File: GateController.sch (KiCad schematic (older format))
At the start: 19 parts, among them K1 RAYEX-L90, K2 RAYEX-L90, M1 N-CHANNEL-MOSFET-BSS138, M2 N-CHANNEL-MOSFET-BSS138, M3 Motor_DC, P1 Power, P2 Analog, P3 Digital, P4 Digital, P5 CONN_01X01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

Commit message: Added pages for power and inputs
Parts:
- removed C1: C_Small, symbol Device:C_Small
- removed D3: DIODE, symbol AM2:DIODE-Microtan_65_CPU-cache
- removed D4: DIODE, symbol pspice:DIODE
- removed R1: R_Small, symbol Device:R_Small
- D1, D2: symbol AM2:DIODE-Microtan_65_CPU-cache -> GateController-rescue:DIODE-Microtan_65_CPU-cache-AM2
- M1, M2: symbol AM1:GeekAmmo_N-CHANNEL-MOSFET-BSS138 -> GateController-rescue:GeekAmmo_N-CHANNEL-MOSFET-BSS138-AM1
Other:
- note removed: "INPUT"
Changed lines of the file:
@@
 $Descr A4 11693 8268
 encoding utf-8
-Sheet 1 1
+Sheet 1 3
 Title ""
 Date "lun. 30 mars 2015"
@@
 	10700 1000 10700 500
 $Comp
-L Device:R_Small R1
-U 1 1 5F5FCCF6
-P 6650 5550
-F 0 "R1" V 6454 5550 50  0000 C CNN
-F 1 "R_Small" V 6545 5550 50  0000 C CNN
-F 2 "" H 6650 5550 50  0001 C CNN
-F 3 "~" H 6650 5550 50  0001 C CNN
-	1    6650 5550
-	0    -1   1    0
-$EndComp
-$Comp
-L AM2:DIODE-Microtan_65_CPU-cache D3
-U 1 1 5F5FD3D3
-P 6250 5250
-F 0 "D3" V 6288 5172 40  0000 R CNN
-F 1 "DIODE" V 6212 5172 40  0000 R CNN
-F 2 "" H 6250 5250 60  0001 C CNN
-F 3 "" H 6250 5250 60  0000 C CNN
-	1    6250 5250
-	0    1    -1   0
-$EndComp
-$Comp
-L power:+5V #PWR0102
-U 1 1 5F5FE717
-P 6250 4850
-F 0 "#PWR0102" H 6250 4700 50  0001 C CNN
-F 1 "+5V" H 6265 5023 50  0000 C CNN
-F 2 "" H 6250 4850 50  0001 C CNN
-F 3 "" H 6250 4850 50  0001 C CNN
-	1    6250 4850
-	-1   0    0    -1
-$EndComp
-$Comp
-L Device:C_Small C1
-U 1 1 5F5FEC7A
-P 5700 5900
-F 0 "C1" H 5792 5946 50  0000 L CNN
-F 1 "C_Small" H 5792 5855 50  0000 L CNN
-F 2 "" H 5700 5900 50  0001 C CNN
-F 3 "~" H 5700 5900 50  0001 C CNN
-	1    5700 5900
-	-1   0    0    -1
-$EndComp
-Wire Wire Line
-	6550 5550 6250 5550
-Wire Wire Line
-	6250 5550 6250 5450
-Connection ~ 6250 5550
-Wire Wire Line
-	6250 5050 6250 4850
-Wire Wire Line
-	6250 5550 5700 5550
-Wire Wire Line
-	5700 5550 5700 5800
-$Comp
-L AM1:Microtan_65_CPU-cache_GND #PWR0103
-U 1 1 5F5FFCD8
-P 5700 6300
-F 0 "#PWR0103" H 5700 6300 30  0001 C CNN
-F 1 "Microtan_65_CPU-cache_GND" H 5700 6230 30  0001 C CNN
-F 2 "" H 5700 6300 60  0000 C CNN
-F 3 "" H 5700 6300 60  0000 C CNN
-	1    5700 6300
-	-1   0    0    -1
-$EndComp
-$Comp
 L Relay:RAYEX-L90 K1
 U 1 1 5F6004E4
@@
 	4200 3150 4050 3150
 $Comp
-L AM2:DIODE-Microtan_65_CPU-cache D1
+L GateController-rescue:DIODE-Microtan_65_CPU-cache-AM2 D1
 U 1 1 5F60A460
 P 3650 2550
@@
 $EndComp
 $Comp
-L AM2:DIODE-Microtan_65_CPU-cache D2
+L GateController-rescue:DIODE-Microtan_65_CPU-cache-AM2 D2
 U 1 1 5F60ADB2
 P 6000 2500
@@
 	6600 3150 6400 3150
 $Comp
-L AM1:GeekAmmo_N-CHANNEL-MOSFET-BSS138 M2
+L GateController-rescue:GeekAmmo_N-CHANNEL-MOSFET-BSS138-AM1 M2
 U 1 1 5F60E051
 P 2100 3400
@@
 $EndComp
 $Comp
-L AM1:GeekAmmo_N-CHANNEL-MOSFET-BSS138 M1
+L GateController-rescue:GeekAmmo_N-CHANNEL-MOSFET-BSS138-AM1 M1
 U 1 1 5F610BFB
 P 1350 3350
@@
 	4200 1850 4200 2550
 Connection ~ 6600 2500
-Text Notes 5900 5050 2    50   ~ 0
-INPUT
 Text Notes 3450 1700 0    50   ~ 0
 MOTOR\nCONTROL
-Wire Wire Line
-	5700 5550 4150 5550
-Connection ~ 5700 5550
-Wire Wire Line
-	6750 5550 7450 5550
 Wire Wire Line
 	1900 3500 1900 4300
@@
 Text Label 4150 5450 0    50   ~ 0
 2
-Text Label 4150 5550 0    50   ~ 0
-5(**)
-Text Label 7450 5550 0    50   ~ 0
-MAGICEYE
 Wire Wire Line
 	4850 1700 4200 1700
@@
 NoConn ~ 8900 2800
 $Comp
-L power:PWR_FLAG #FLG0102
-U 1 1 5F7E15C6
-P 7450 5250
-F 0 "#FLG0102" H 7450 5325 50  0001 C CNN
-F 1 "PWR_FLAG" H 7450 5423 50  0000 C CNN
-F 2 "" H 7450 5250 50  0001 C CNN
-F 3 "~" H 7450 5250 50  0001 C CNN
-	1    7450 5250
-	1    0    0    -1
-$EndComp
-Wire Wire Line
-	7450 5250 7450 5550
-$Comp
 L power:PWR_FLAG #FLG0103
 U 1 1 5F7E9261
@@
 Wire Wire Line
 	10300 3150 10300 3200
-Wire Wire Line
-	6250 5550 6250 5650
-$Comp
-L pspice:DIODE D4
-U 1 1 5F5FD987
-P 6250 5850
-F 0 "D4" V 6288 5772 40  0000 R CNN
-F 1 "DIODE" V 6212 5772 40  0000 R CNN
-F 2 "" H 6250 5850 60  0001 C CNN
-F 3 "" H 6250 5850 60  0000 C CNN
-	1    6250 5850
-	0    1    -1   0
-$EndComp
-Wire Wire Line
-	6250 6050 6250 6300
-$Comp
-L AM1:Microtan_65_CPU-cache_GND #PWR0101
-U 1 1 5F5FE1C8
-P 6250 6300
-F 0 "#PWR0101" H 6250 6300 30  0001 C CNN
-F 1 "Microtan_65_CPU-cache_GND" H 6250 6230 30  0001 C CNN
-F 2 "" H 6250 6300 60  0000 C CNN
-F 3 "" H 6250 6300 60  0000 C CNN
-	1    6250 6300
-	-1   0    0    -1
-$EndComp
 $Comp
 L power:PWR_FLAG #FLG0106
@@
 Wire Wire Line
 	6150 7350 6150 7650
-Wire Wire Line
-	5700 6000 5700 6300
 $Comp
 L power:GNDPWR #PWR0111
@@
 	1    0    0    -1
 $EndComp
+$Sheet
+S 8700 3650 850  550
+U 5F62F258
+F0 "Sheet5F62F257" 50
+F1 "gate_ctrl_inputs.sch" 50
+$EndSheet
+$Sheet
+S 8750 4550 850  550
+U 5F648DDC
+F0 "Sheet5F648DDB" 50
+F1 "gate_ctrl_power.sch" 50
+$EndSheet
 $EndSCHEMATC

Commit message: Added outputs page, leds.
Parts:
- added D? (x2): LED, symbol Device:LED
- added R? (x2): R_Small, symbol Device:R_Small
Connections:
- net +24V: now also D?.1 (K), D?.1 (K)
- net at D1.1 (A), K1.A1, M2.3 (D): now also R?.2
- net at D2.1 (A), K2.A2, M1.3 (D): now also R?.2
- new net: D?.2 (A), R?.1 (x2)
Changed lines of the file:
@@
 $Descr A4 11693 8268
 encoding utf-8
-Sheet 1 3
+Sheet 1 4
 Title ""
 Date "lun. 30 mars 2015"
@@
 	4200 1850 6600 1850
 Wire Wire Line
-	6600 1850 6600 2500
+	6600 1850 6600 2200
 Connection ~ 4200 1850
 Wire Wire Line
-	4200 1850 4200 2550
+	4200 1850 4200 2000
 Connection ~ 6600 2500
 Text Notes 3450 1700 0    50   ~ 0
@@
 F1 "gate_ctrl_power.sch" 50
 $EndSheet
+$Sheet
+S 8850 5400 950  550
+U 5F669EA7
+F0 "Sheet5F669EA6" 50
+F1 "gate_ctrl_outputs.sch" 50
+$EndSheet
+$Comp
+L Device:LED D?
+U 1 1 5F682773
+P 6250 2200
+F 0 "D?" H 6243 1945 50  0000 C CNN
+F 1 "LED" H 6243 2036 50  0000 C CNN
+F 2 "" H 6250 2200 50  0001 C CNN
+F 3 "~" H 6250 2200 50  0001 C CNN
+	1    6250 2200
+	-1   0    0    1
+$EndComp
+$Comp
+L Device:LED D?
+U 1 1 5F6837F7
+P 3950 2000
+F 0 "D?" H 3943 1745 50  0000 C CNN
+F 1 "LED" H 3943 1836 50  0000 C CNN
+F 2 "" H 3950 2000 50  0001 C CNN
+F 3 "~" H 3950 2000 50  0001 C CNN
+	1    3950 2000
+	-1   0    0    1
+$EndComp
+Wire Wire Line
+	4100 2000 4200 2000
+Connection ~ 4200 2000
+Wire Wire Line
+	4200 2000 4200 2550
+Wire Wire Line
+	6400 2200 6600 2200
+Connection ~ 6600 2200
+Wire Wire Line
+	6600 2200 6600 2500
+$Comp
+L Device:R_Small R?
+U 1 1 5F68A7C5
+P 5800 2200
+F 0 "R?" V 5604 2200 50  0000 C CNN
+F 1 "R_Small" V 5695 2200 50  0000 C CNN
+F 2 "" H 5800 2200 50  0001 C CNN
+F 3 "~" H 5800 2200 50  0001 C CNN
+	1    5800 2200
+	0    1    1    0
+$EndComp
+$Comp
+L Device:R_Small R?
+U 1 1 5F68B356
+P 3500 2000
+F 0 "R?" V 3304 2000 50  0000 C CNN
+F 1 "R_Small" V 3395 2000 50  0000 C CNN
+F 2 "" H 3500 2000 50  0001 C CNN
+F 3 "~" H 3500 2000 50  0001 C CNN
+	1    3500 2000
+	0    1    1    0
+$EndComp
+Wire Wire Line
+	3600 2000 3800 2000
+Wire Wire Line
+	3400 2000 3150 2000
+Wire Wire Line
+	3150 2000 3150 2550
+Connection ~ 3150 2550
+Wire Wire Line
+	6100 2200 5900 2200
+Wire Wire Line
+	5700 2200 5500 2200
+Wire Wire Line
+	5500 2200 5500 2500
+Connection ~ 5500 2500
 $EndSCHEMATC

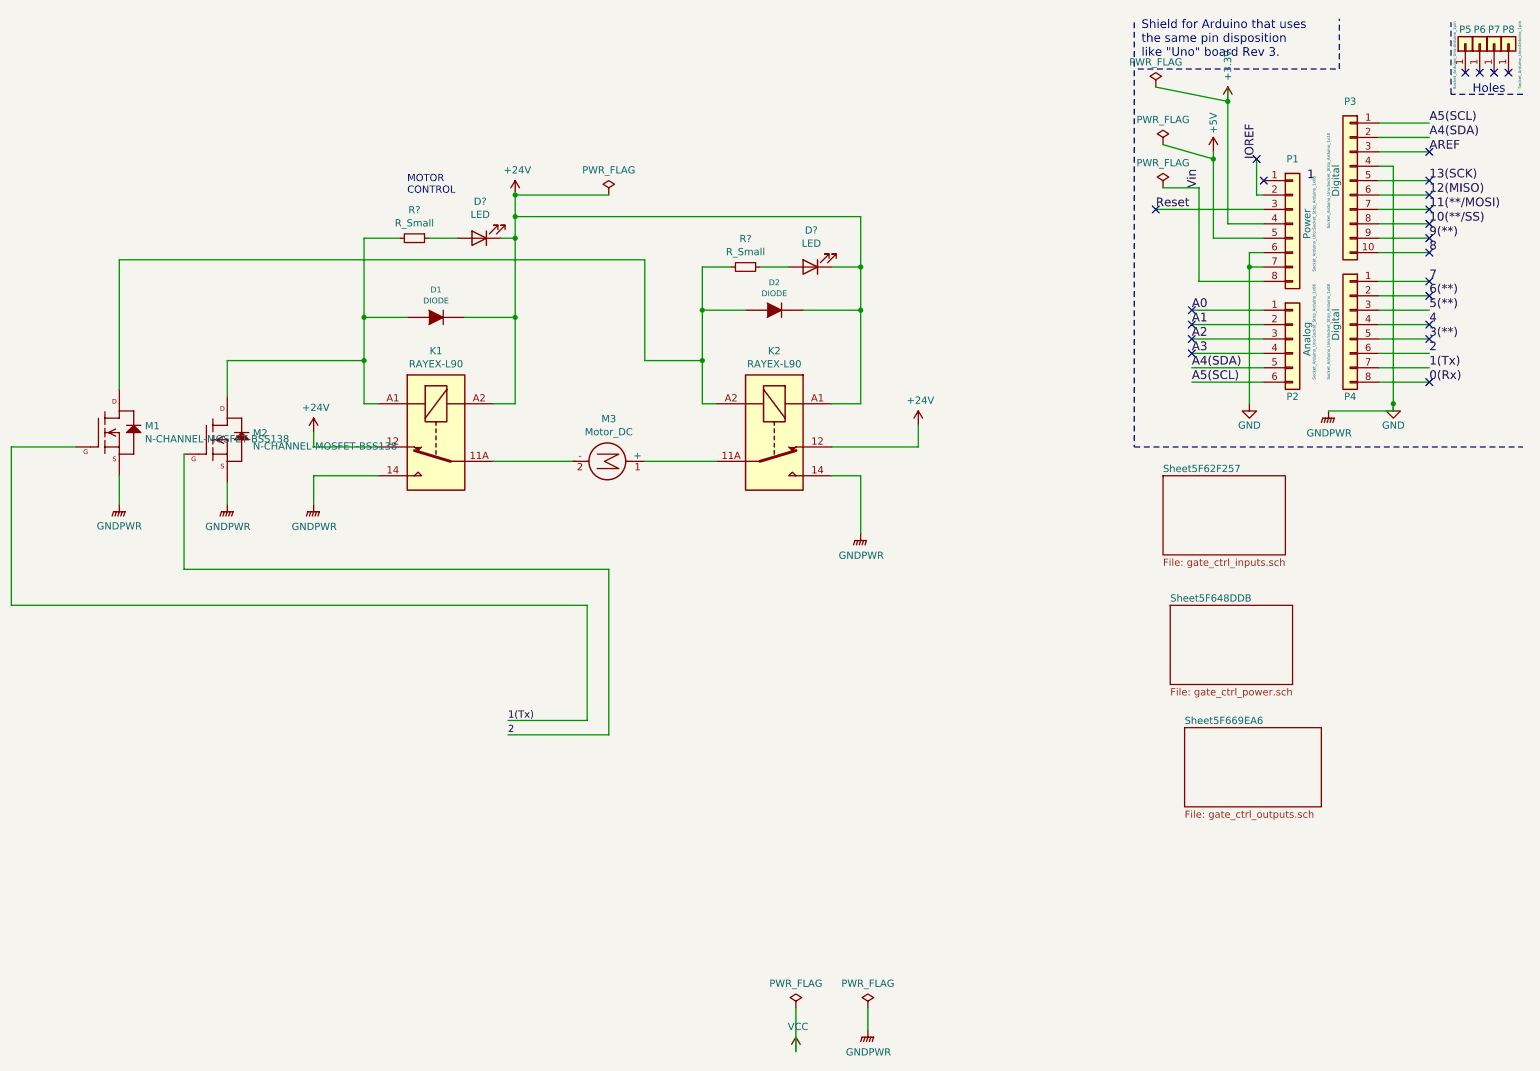
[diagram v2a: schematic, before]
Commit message: Added OLED and RF data input
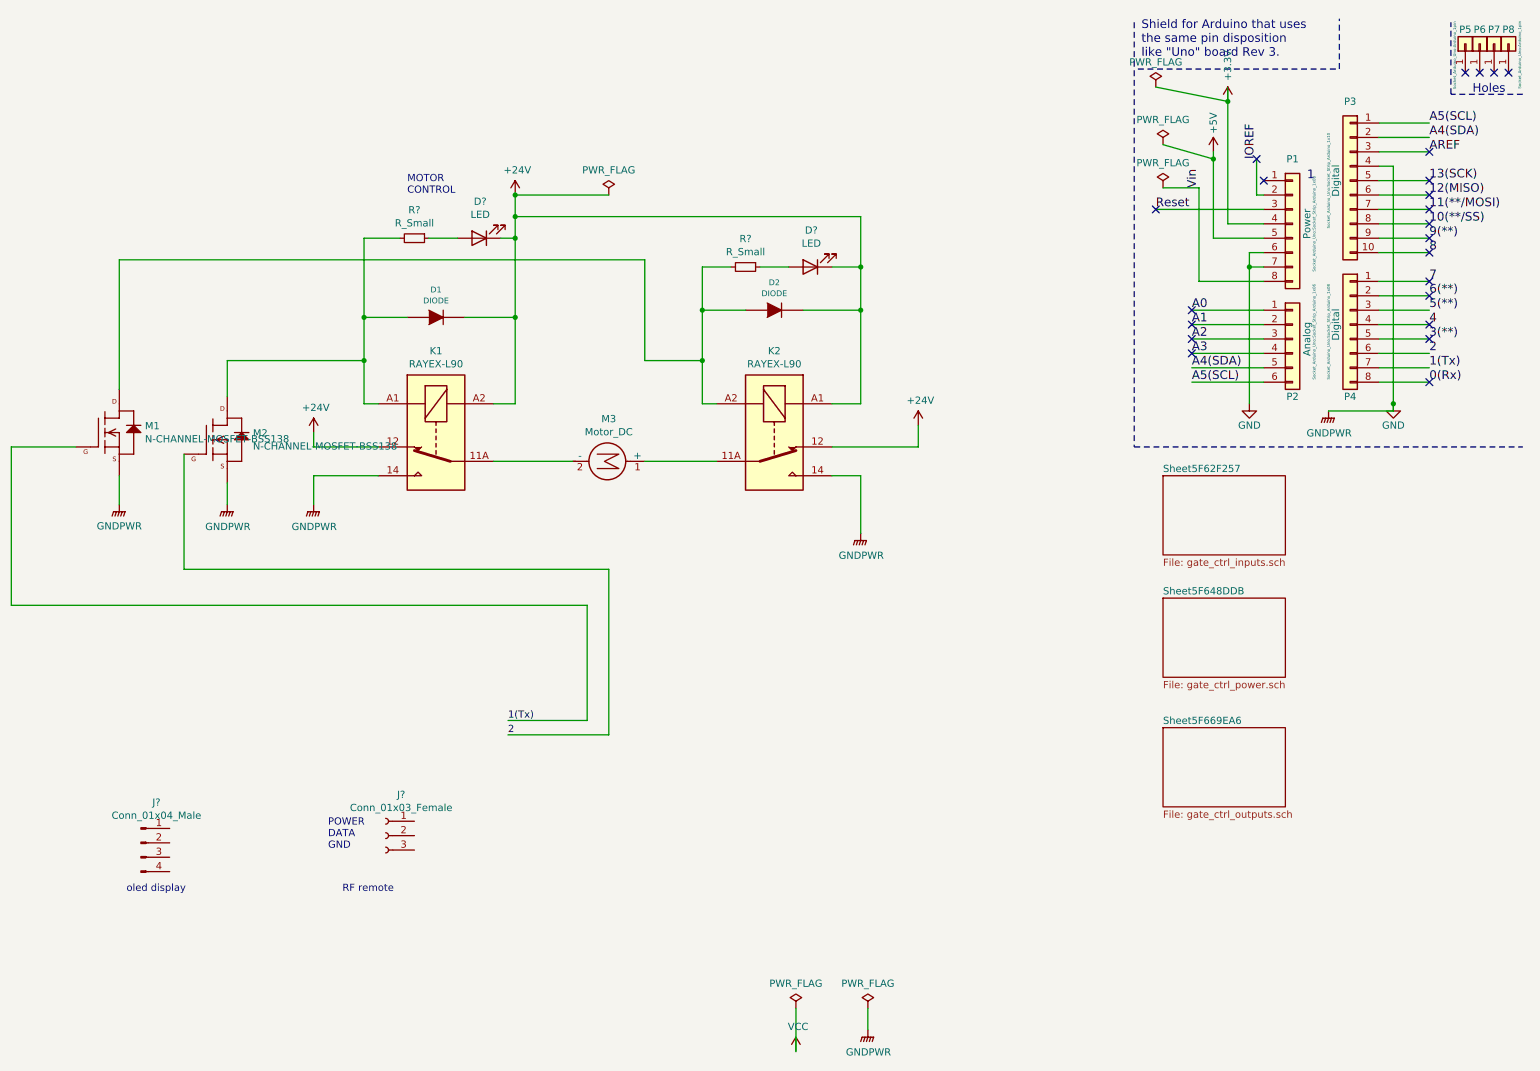
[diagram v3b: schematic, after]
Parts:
- added J?: Conn_01x04_Male, symbol Connector:Conn_01x04_Male
- added J?: Conn_01x03_Female, symbol Connector:Conn_01x03_Female
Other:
- note added: "POWER\nDATA\nGND"
- note added: "RF remote\n"
- note added: "oled display"
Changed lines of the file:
@@
 $EndSheet
 $Sheet
-S 8750 4550 850  550
+S 8700 4500 850  550
 U 5F648DDC
 F0 "Sheet5F648DDB" 50
@@
 $EndSheet
 $Sheet
-S 8850 5400 950  550
+S 8700 5400 850  550
 U 5F669EA7
 F0 "Sheet5F669EA6" 50
@@
 	5500 2200 5500 2500
 Connection ~ 5500 2500
+$Comp
+L Connector:Conn_01x04_Male J?
+U 1 1 5F6FF403
+P 1600 6200
+F 0 "J?" H 1708 6481 50  0000 C CNN
+F 1 "Conn_01x04_Male" H 1708 6390 50  0000 C CNN
+F 2 "" H 1600 6200 50  0001 C CNN
+F 3 "~" H 1600 6200 50  0001 C CNN
+	1    1600 6200
+	1    0    0    -1
+$EndComp
+Text Notes 1500 6550 0    50   ~ 0
+oled display
+$Comp
+L Connector:Conn_01x03_Female J?
+U 1 1 5F701695
+P 3300 6150
+F 0 "J?" H 3192 6435 50  0000 C CNN
+F 1 "Conn_01x03_Female" H 3192 6344 50  0000 C CNN
+F 2 "" H 3300 6150 50  0001 C CNN
+F 3 "~" H 3300 6150 50  0001 C CNN
+	1    3300 6150
+	-1   0    0    -1
+$EndComp
+Text Notes 3000 6550 0    50   ~ 0
+RF remote\n
+Text Notes 2900 6250 0    50   ~ 0
+POWER\nDATA\nGND
 $EndSCHEMATC
